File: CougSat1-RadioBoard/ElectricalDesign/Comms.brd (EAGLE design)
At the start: 90.4 x 95.8 mm, 416 parts, among them J1 230mm Antenna, J2 CougSat Card, J3 700mm Antenna, J4 SWD, Q1 CSD25402Q3A, Q12 DMN53D0LDW, Q2 CSD25402Q3A, Q3 DMN53D0LDW, Q9 DMN53D0LDW, U1 INA199C1, U10 HMC452QS16G, U11 AD8515, U12 AD7291, U13 AD8515, U14 LP5907MFX-3.1, U15 AD9761, U16 TXS0102DQM, U18 TXS0102DQM, U19 MMZ09332B, U2 LP5907MFX-3.1, U20 ADF4360, U21 HMC545A, U22 AD9761, U23 MAAM-011229, U24 AD8515, U25 MAAM-011229, U26 AD8345, U28 AD8348, U29 AD7291, U3 TPS61236, U30 TXS0102DQM, U31 MAAM-011229, U32 AD8515, U35 TXS0102DQM, U36 ADF4360, U37 MAAM-011229, U39 AD8515, U4 AD8346, U40 AD8515, U42 TXS0102DQM, U43 INA199C2, U44 TXS0102DQM, U45 TXS0102DQM, U46 TXS0102DQM, U47 TXS0102DQM, U48 AD7291, U49 AD8515, U5 ADF4360, U50 INA199C2, U51 LP5907MFX-3.1, U52 INA199C2, U53 INA199C1, U54 TXS0102DQM, U55 TXS0102DQM, U6 STM32L496VGT, U7 GRF2133, U8 IS25LP016D, U9 IS25LP016D, Y1 19.68MHz ±2.5ppm, Y2 8MHz ±10ppm, Y3 32.768kHz ±10ppm, Y4 19.68MHz ±2.5ppm, Y5 19.68MHz ±2.5ppm

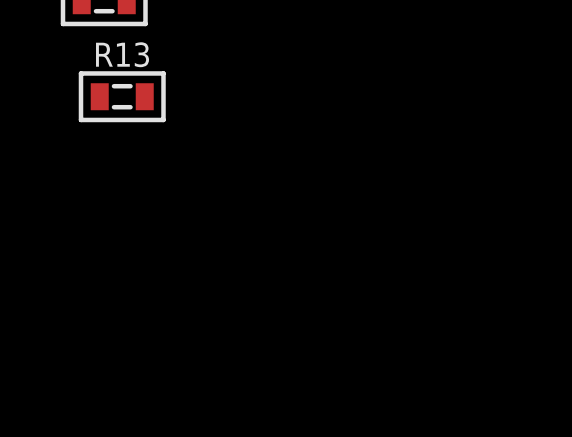
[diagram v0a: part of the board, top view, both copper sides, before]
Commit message: Updated layout constraints and tests
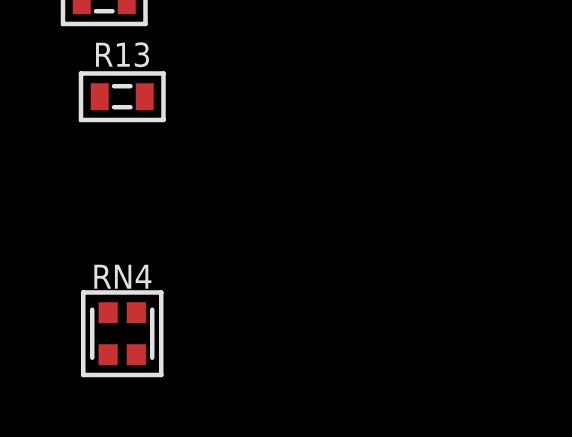
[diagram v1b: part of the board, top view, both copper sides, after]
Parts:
- added RN4: 5kΩ 0.1%, CougsInSpace-Resistors:1616
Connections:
- net PA_PDET-700: now also RN4.2
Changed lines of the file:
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@@
 <attribute name="TEMP" value="70°C Max 2A" x="-84.8" y="-289.1" size="0.8" layer="27" font="vector" ratio="15" display="off"/>
 </element>
+<element name="RN4" library="CougsInSpace-Resistors" package="1616" value="5kΩ 0.1%" x="-84.8" y="-297" smashed="yes">
+<attribute name="NAME" x="-84.8" y="-295.1" size="0.8" layer="25" font="vector" ratio="15" align="center"/>
+<attribute name="PACKAGE" value="1616" x="-84.8" y="-297" size="0.8" layer="27" font="vector" ratio="15" display="off"/>
+<attribute name="POWER" value="1/8W" x="-84.8" y="-297" size="0.8" layer="27" font="vector" ratio="15" display="off"/>
+<attribute name="SKU" value="26-0007" x="-84.8" y="-297" size="0.8" layer="27" font="vector" ratio="15" display="off"/>
+<attribute name="TEMP" value="±10ppm/°C" x="-84.8" y="-297" size="0.8" layer="27" font="vector" ratio="15" display="off"/>
+</element>
 </elements>
 <signals>
@@
 <contactref element="U32" pad="1"/>
 <contactref element="U32" pad="4"/>
+<contactref element="RN4" pad="2"/>
 <wire x1="-77.29" y1="-139.55" x2="-79.91" y2="-137.65" width="0" layer="19" extent="1-1"/>
+<wire x1="-84.33" y1="-297.7" x2="-77.29" y2="-139.55" width="0" layer="19" extent="1-1"/>
 </signal>
 <signal name="PA_RFOUT-700">

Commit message: Began part placement
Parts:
- moved C20 461.0 mm to (38.0, 161.5), turned to 90 degrees
- moved RN4 450.6 mm to (102.2, 113.0)
- moved RT2 361.4 mm to (-7.70, 67.0), turned to 90 degrees
- moved R20 336.9 mm to (-10.4, 49.1)
- moved C58 317.0 mm to (-15.4, 141.6)
- moved RT1 316.9 mm to (-8.80, 31.2), turned to 90 degrees
- moved R13 311.1 mm to (9.50, 7.40), turned to 180 degrees
- moved C109 310.1 mm to (-11.0, 37.7)
- moved U18 309.7 mm to (-94.5, 121.1)
- moved C54 309.7 mm to (-10.7, 45.0), turned to 270 degrees
- moved R87 309.0 mm to (-10.4, 47.4)
- moved U50 307.7 mm to (-15.4, 139.1), turned to 270 degrees
- moved L21 307.3 mm to (-14.5, 53.0)
- moved U16 306.5 mm to (-97.4, 121.1)
- moved R19 306.4 mm to (-8.90, 23.7)
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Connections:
- removed net 3.3V_2: U20.2, U20.21, U20.23, U20.6
- removed net PR_3.3V-0: J2.A1, J2.B1
- net 3.1V_2: now also U20.2, U20.21, U20.23, U20.6
- net 3.3V_0: now also J2.A1, J2.B1; no longer J2.A40, J2.B40
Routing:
- net PGND: track 936.1 -> 42.8 mm, vias 273 -> 3
- net RFGND-1: track 807.1 -> 0.00 mm, vias 160 -> 0
- net DGND: track 694.2 -> 0.00 mm, vias 143 -> 0
- net AVDD: track 624.3 -> 0.00 mm, vias 34 -> 0
- net RFGND-0: track 431.6 -> 0.00 mm, vias 90 -> 0
- net AGND: track 431.2 -> 0.00 mm, vias 104 -> 0
- net CHASSIS_230-0: track 146.3 -> 0.00 mm, vias 2 -> 0
- net 3.1V_1: track 103.8 -> 0.00 mm, vias 13 -> 0
- net TEMP_CLK_MOD: track 102.2 -> 0.00 mm, vias 1 -> 0
- net MUXOUT-MOD: track 92.6 -> 0.00 mm, vias 2 -> 0
- net CHASSIS_700-1: track 92.1 -> 0.00 mm
- net MOD_700_QD_P: track 82.2 -> 0.00 mm
- net MOD_700_ID_N: track 81.3 -> 0.00 mm, vias 2 -> 0
- net MOD_700_QD_N: track 81.1 -> 0.00 mm
- net MOD_700_ID_P: track 80.3 -> 0.00 mm, vias 2 -> 0
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- removed copper zone on layer 1, net !COM_SPI_CS
- removed copper zone on layer 1, net 3.3V
- removed copper zone on layer 15, net 3.3V
- removed copper zone on layer 1, net 3.3V_0
- removed copper zone on layer 15, net 3.3V_0
- removed copper zone on layer 15, net 3.3V_1
- removed copper zone on layer 1, net 3.3V_2
- removed copper zone on layer 15, net 3.3V_2
- removed copper zone on layer 1, net 5.0V
- removed copper zone on layer 15, net 5.0V
- removed copper zone on layer 1, net 5.0V_0
- removed copper zone on layer 15, net 5.0V_0
- removed copper zone on layer 15, net 5.0V_1
- removed copper zone on layer 15, net 5.0V_2
- removed copper zone on layer 1, net 5.0V_I
- removed copper zone on layer 1, net 9.0V
- removed copper zone on layer 15, net 9.0V
- removed copper zone on layer 1, net 9.0V_0
- removed copper zone on layer 15, net 9.0V_0
- removed copper zone on layer 1, net 9.0V_1
- removed copper zone on layer 15, net 9.0V_1
- removed copper zone on layer 1, net 9.0V_I
- removed copper zone on layer 1, net AGND
- removed copper zone on layer 16, net AGND
- removed copper zone on layer 2, net AGND
- removed copper zone on layer 15, net AVDD
- removed copper zone on layer 15, net AVDD_NEG
- removed copper zone on layer 1, net BUS_JTAG_TCK
- removed copper zone on layer 1, net BUS_JTAG_TDI
- removed copper zone on layer 1, net BUS_JTAG_TDO
- removed copper zone on layer 1, net BUS_JTAG_TMS
- removed copper zone on layer 1, net CHASSIS
- removed copper zone on layer 16, net CHASSIS
- removed copper zone on layer 1, net COM_SPI_MISO
- removed copper zone on layer 1, net COM_SPI_MOSI
- removed copper zone on layer 1, net COM_SPI_SCK
- removed copper zone on layer 1, net CTRL_!RESET
- removed copper zone on layer 1, net CTRL_SYNC
- removed copper zone on layer 1, net DGND
- removed copper zone on layer 15, net DGND
- removed copper zone on layer 16, net DGND
- removed copper zone on layer 2, net DGND
- removed copper zone on layer 1, net I_3.3V-0P
- removed copper zone on layer 1, net I_3.3V-1P
- removed copper zone on layer 1, net I_3.3V-2P
- removed copper zone on layer 1, net I_5.0V-1P
- removed copper zone on layer 1, net I_5.0V-2P
- removed copper zone on layer 1, net I_9.0V_0
- removed copper zone on layer 1, net I_9.0V_1
- removed copper zone on layer 16, net JTAG_EN_COMMS
- removed copper zone on layer 1, net PGND
- removed copper zone on layer 15, net PGND
- removed copper zone on layer 16, net PGND
- removed copper zone on layer 2, net PGND
- removed copper zone on layer 1, net REG_SW-5
- removed copper zone on layer 1, net REG_SW-9
- removed copper zone on layer 1, net RFGND-0
- removed copper zone on layer 15, net RFGND-0
- removed copper zone on layer 16, net RFGND-0
- removed copper zone on layer 2, net RFGND-0
- removed copper zone on layer 1, net RFGND-1
- removed copper zone on layer 15, net RFGND-1
- removed copper zone on layer 16, net RFGND-1
- removed copper zone on layer 2, net RFGND-1
- removed copper zone on layer 1, net VBATT
- removed copper zone on layer 15, net VBATT
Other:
- board text removed: "Comms V1.0 1901"

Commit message: Placed Comms parts
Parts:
- H4: value 230mm RF Shield -> Can - 230mm; device CougsInSpace-Hardware:SHIELD-2626 -> CougsInSpace-Hardware:SHIELD-2641
- H7: value Analog Shield -> Can - Modulator; device CougsInSpace-Hardware:SHIELD-3044 -> CougsInSpace-Hardware:SHIELD-2641
- H8: value 700mm RF Shield -> Can - Demodulator; device CougsInSpace-Hardware:SHIELD-3044 -> CougsInSpace-Hardware:SHIELD-2641
- moved FB4 223.9 mm to (74.6, 27.8), turned to 270 degrees
- moved R61 222.4 mm to (73.5, 21.4), turned to 90 degrees
- moved C72 221.8 mm to (74.6, 30.7)
- moved C49 221.4 mm to (36.0, -43.3), turned to 270 degrees
- moved C48 219.2 mm to (28.2, -41.4), turned to 90 degrees
- moved C80 219.1 mm to (71.8, 21.4), turned to 270 degrees
- moved C62 217.6 mm to (71.8, 25.4), turned to 180 degrees
- moved C75 217.4 mm to (71.4, 23.7), turned to 180 degrees
- moved Y4 216.6 mm to (71.8, 28.5), turned to 270 degrees
- moved R28 216.4 mm to (28.2, -38.5), turned to 90 degrees
- moved R69 215.6 mm to (69.5, 19.1), turned to 180 degrees
- moved C158 215.3 mm to (2.90, -34.9), turned to 90 degrees
- moved R29 215.3 mm to (20.6, -39.4)
- moved L9 214.8 mm to (69.5, 20.8), turned to 180 degrees
- moved U8 214.3 mm to (32.2, -40.1), turned to 270 degrees
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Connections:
- net DGND: no longer H7.1, H7.10, H7.11, H7.12, H7.13, H7.14, H7.15, H7.16, H7.17, H7.18, H7.19, H7.2, H7.20, H7.21, H7.22, H7.23, H7.24, H7.25, H7.26, H7.27, H7.28, H7.3, H7.4, H7.5, H7.6, H7.7, H7.8, H7.9
- net RFGND-0: no longer H4.10, H4.11, H4.12, H4.13, H4.14, H4.15, H4.16, H4.17, H4.18, H4.19, H4.20, H4.3, H4.4, H4.5, H4.6, H4.7, H4.8, H4.9
- net RFGND-1: now also H7.1, H7.2; no longer H8.10, H8.11, H8.12, H8.13, H8.14, H8.15, H8.16, H8.17, H8.18, H8.19, H8.20, H8.21, H8.22, H8.23, H8.24, H8.25, H8.26, H8.27, H8.28, H8.3, H8.4, H8.5, H8.6, H8.7, H8.8, H8.9
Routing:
- net MOD_PA_230_RFOUT: track 0.69 -> 0.05 mm

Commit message: Laid out RF traces
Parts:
- removed C13, C40: 100nF 10%, CougsInSpace-Capacitors:1608
- removed H1, H3: M2, CougsInSpace-Hardware:MOUNTING_HOLE-2.2
- removed R17, R9: 0Ω <20mΩ, CougsInSpace-Resistors:1608
- moved LOGO1 200.0 mm to (-13.9, 1.60)
- moved LOGO2 200.0 mm to (-14.4, -35.6)
- moved LOGO3 200.0 mm to (-13.5, -14.0)
- moved C164 1.60 mm to (79.1, -24.9)
- moved C71 0.72 mm to (60.5, -1.30)
- moved L19 0.72 mm to (60.5, -3.00)
- moved C53 0.70 mm to (85.8, -24.9)
- moved L5 0.70 mm to (82.9, -24.9)
- moved C82 0.67 mm to (59.7, -5.30)
- moved FB5 0.45 mm to (80.5, 35.0)
- moved C117 0.45 mm to (68.7, 35.2)
- moved C124 0.45 mm to (68.7, 33.5)
- moved C107 0.45 mm to (68.7, 37.0)
- moved C77 0.43 mm to (80.2, 19.4), turned to 45 degrees
- moved L4 0.34 mm to (84.0, -41.4), turned to 110 degrees
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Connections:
- removed net CHASSIS_REG-0: C40.1, H3.1, H3.V1, H3.V2, H3.V3, H3.V4, H3.V5, H3.V6, H3.V7, H3.V8, R17.2
- removed net CHASSIS_REG-1: C13.1, H1.1, H1.V1, H1.V2, H1.V3, H1.V4, H1.V5, H1.V6, H1.V7, H1.V8, R9.2
- net PGND: no longer C13.2, C40.2, R17.1, R9.1
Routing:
- net RFCLK_OUT-MOD_N: track 0.00 -> 13.0 mm
- net RFCLK_OUT-DEMOD_N: track 0.00 -> 12.8 mm
- net MOD_700_RFOUT: track 0.00 -> 12.6 mm
- net RFCLK_OUT-230_N: track 0.00 -> 12.3 mm
- net RFCLK_OUT-MOD_P: track 0.00 -> 12.2 mm
- net RFCLK_OUT-DEMOD_P: track 0.00 -> 12.0 mm
- net RFCLK_OUT-230_P: track 0.00 -> 11.4 mm
- net MOD_230_RFOUT: track 0.00 -> 10.9 mm
- net MOD_PA_230_RFOUT: track 0.05 -> 10.4 mm
- net MOD_PA_700_RFINMID: track 0.00 -> 9.47 mm
- net RX_LNA_RFOUT-1: track 0.00 -> 6.64 mm
- net ANTENNA_700_TX: track 0.00 -> 6.41 mm
- net DEMOD_700_BALUN_SCT: track 0.00 -> 5.36 mm
- net PA_RFOUT-700: track 0.00 -> 5.36 mm
- net MOD_LNA_230_RFINMID2: track 0.00 -> 4.53 mm
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- added copper zone on layer 1, net ANTENNA_230_COAX
- added copper zone on layer 1, net ANTENNA_700_RX
- added copper zone on layer 1, net ANTENNA_700_TX
- added copper zone on layer 1, net DEMOD_700_BALUN_PRIMARY_DOT1
- added copper zone on layer 1, net DEMOD_700_LOI_N
- added copper zone on layer 1, net DEMOD_700_LOI_P
- added copper zone on layer 1, net DEMOD_RF
- added copper zone on layer 1, net MOD_230_RFOUT
- added copper zone on layer 1, net MOD_700_RFOUT
- added copper zone on layer 1, net MOD_LNA_230_RFINMID1
- added copper zone on layer 1, net MOD_LNA_230_RFINMID2
- added copper zone on layer 1, net MOD_LNA_230_RFOUT
- added copper zone on layer 1, net MOD_LNA_700_RFIN
- added copper zone on layer 1, net MOD_LNA_700_RFINMID
- added copper zone on layer 1, net MOD_LNA_700_RFOUT
- added copper zone on layer 1, net MOD_PA_230_RFIN
- added copper zone on layer 1, net MOD_PA_230_RFINMID
- added copper zone on layer 1, net MOD_PA_230_RFOUT
- added copper zone on layer 1, net MOD_PA_700_RFIN
- added copper zone on layer 1, net MOD_PA_700_RFINMID
- added copper zone on layer 1, net PA_RFOUT-700
- added copper zone on layer 1, net PA_RFOUTMID-700
- added copper zone on layer 1, net RFCLK_OUT-230_N
- added copper zone on layer 1, net RFCLK_OUT-230_P
- added copper zone on layer 1, net RFCLK_OUT-DEMOD_N
- added copper zone on layer 1, net RFCLK_OUT-DEMOD_P
- added copper zone on layer 1, net RFCLK_OUT-MOD_N
- added copper zone on layer 1, net RFCLK_OUT-MOD_P
- added copper zone on layer 1, net RX_LNA_RFIN-0
- added copper zone on layer 1, net RX_LNA_RFIN-1
- added copper zone on layer 1, net RX_LNA_RFIN-2
- added copper zone on layer 1, net RX_LNA_RFOUT-0
- added copper zone on layer 1, net RX_LNA_RFOUT-1

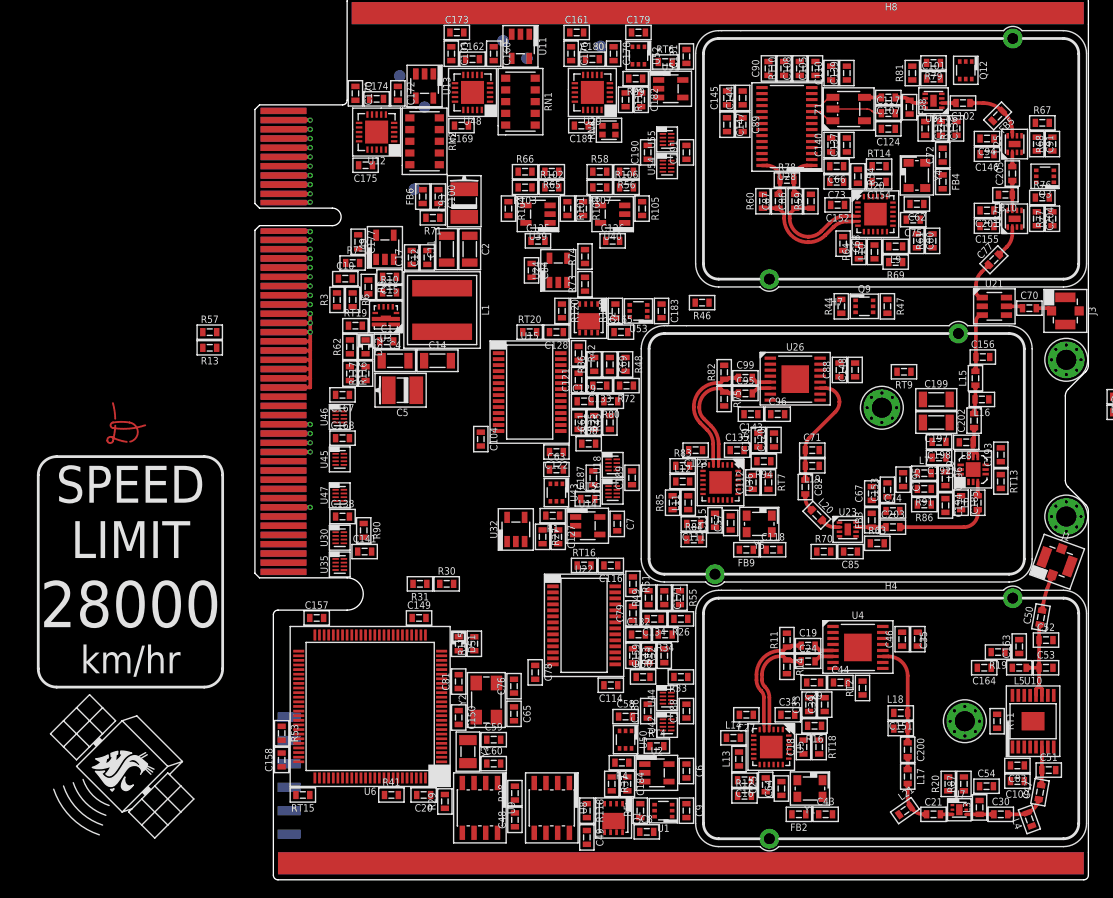
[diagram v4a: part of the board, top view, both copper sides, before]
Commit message: Laid out decapaps for the RF chips
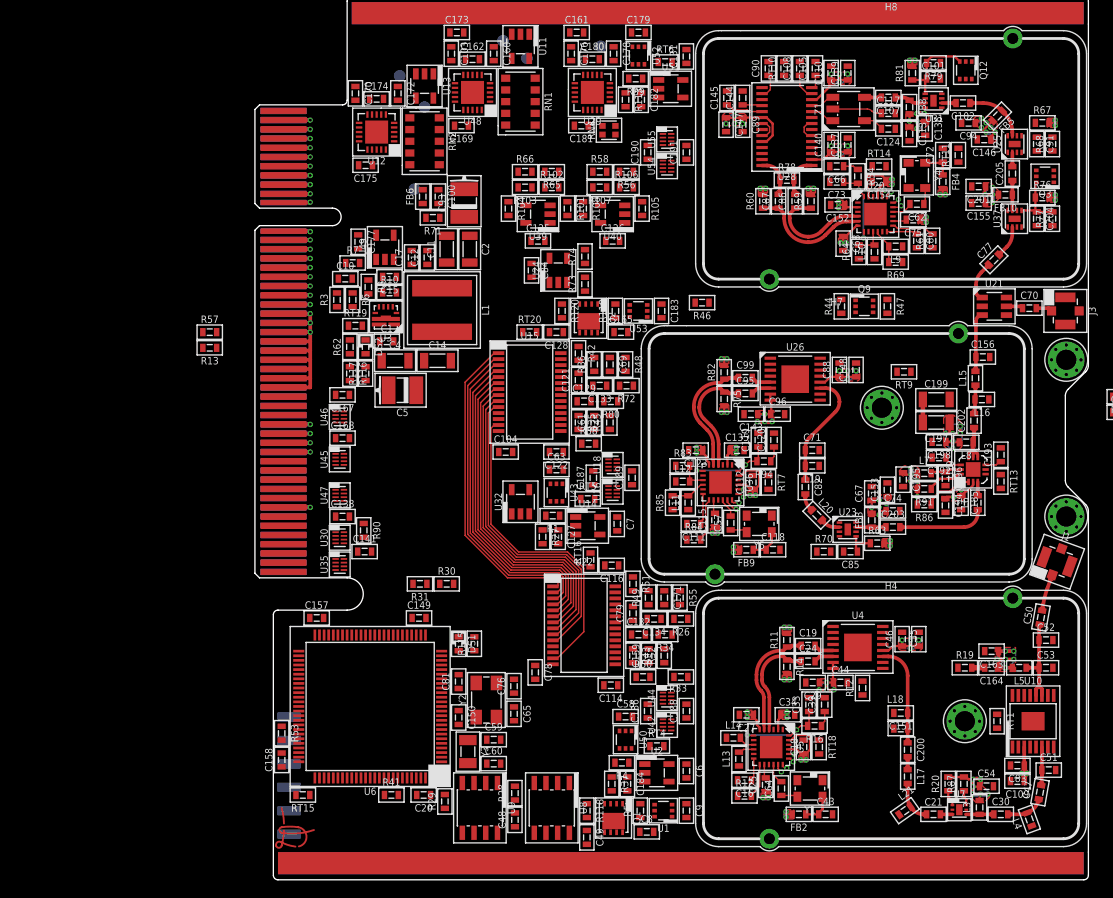
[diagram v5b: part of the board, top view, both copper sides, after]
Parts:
- moved LOGO3 56.3 mm to (34.5, 15.4), flipped to the bottom
- moved LOGO2 53.6 mm to (31.3, -7.60), flipped to the bottom
- moved LOGO1 47.6 mm to (4.40, -42.3)
- moved R19 3.98 mm to (77.0, -24.9), turned to 0 degrees
- moved C163 3.04 mm to (79.9, -23.1), turned to 180 degrees
- moved U32 3.04 mm to (28.8, -6.90)
- moved C104 3.04 mm to (27.2, -1.50), turned to 0 degrees
- moved RT11 2.91 mm to (76.3, 30.7)
- moved C201 2.75 mm to (78.5, 27.3)
- moved C155 2.66 mm to (78.5, 25.5)
- moved C94 2.62 mm to (77.4, 34.2)
- moved C113 1.80 mm to (71.0, 33.0)
- moved C136 1.70 mm to (72.7, 33.6)
- moved C146 1.63 mm to (79.1, 32.4)
- moved RT16 0.92 mm to (36.4, -13.2), turned to 90 degrees
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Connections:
- net RFGND-1: now also Q3.3, Q3.4, Q3.5
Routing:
- net 3.1V_2: track 0.00 -> 63.4 mm, vias 0 -> 47
- net 3.1V_1: track 0.00 -> 39.1 mm, vias 0 -> 29
- net DAC_BUS_8: track 0.00 -> 34.9 mm
- net DAC_BUS_4: track 0.00 -> 34.9 mm
- net DAC_BUS_9: track 0.00 -> 34.9 mm
- net DAC_BUS_7: track 0.00 -> 34.9 mm
- net DAC_BUS_5: track 0.00 -> 34.9 mm
- net DAC_BUS_0: track 0.00 -> 34.9 mm
- net DAC_SELECT_I/!Q: track 0.00 -> 34.9 mm
- net DAC_BUS_6: track 0.00 -> 34.9 mm
- net DAC_BUS_3: track 0.00 -> 34.9 mm
- net DAC_BUS_2: track 0.00 -> 34.9 mm
- net DAC_BUS_1: track 0.00 -> 34.9 mm
- net 3.1V_0: track 0.00 -> 30.8 mm, vias 0 -> 22
- net 5.0V_0: track 0.00 -> 19.5 mm, vias 0 -> 14
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- added copper zone on layer 1, net 3.1V_0
- added copper zone on layer 16, net 3.1V_0
- added copper zone on layer 2, net 3.1V_0
- added copper zone on layer 1, net 3.1V_1
- added copper zone on layer 16, net 3.1V_1
- added copper zone on layer 2, net 3.1V_1
- added copper zone on layer 1, net 3.1V_2
- added copper zone on layer 16, net 3.1V_2
- added copper zone on layer 2, net 3.1V_2
- added copper zone on layer 1, net 5.0V_0
- added copper zone on layer 16, net 5.0V_0
- added copper zone on layer 2, net 5.0V_0
- added copper zone on layer 1, net 5.0V_1
- added copper zone on layer 16, net 5.0V_1
- added copper zone on layer 2, net 5.0V_1
